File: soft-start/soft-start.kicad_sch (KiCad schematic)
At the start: 29 parts, among them M1 Motor_DC, Q1 IRFB3004PbF, SW1 L1's relay switch, U1 4011, U2 CD4060BE

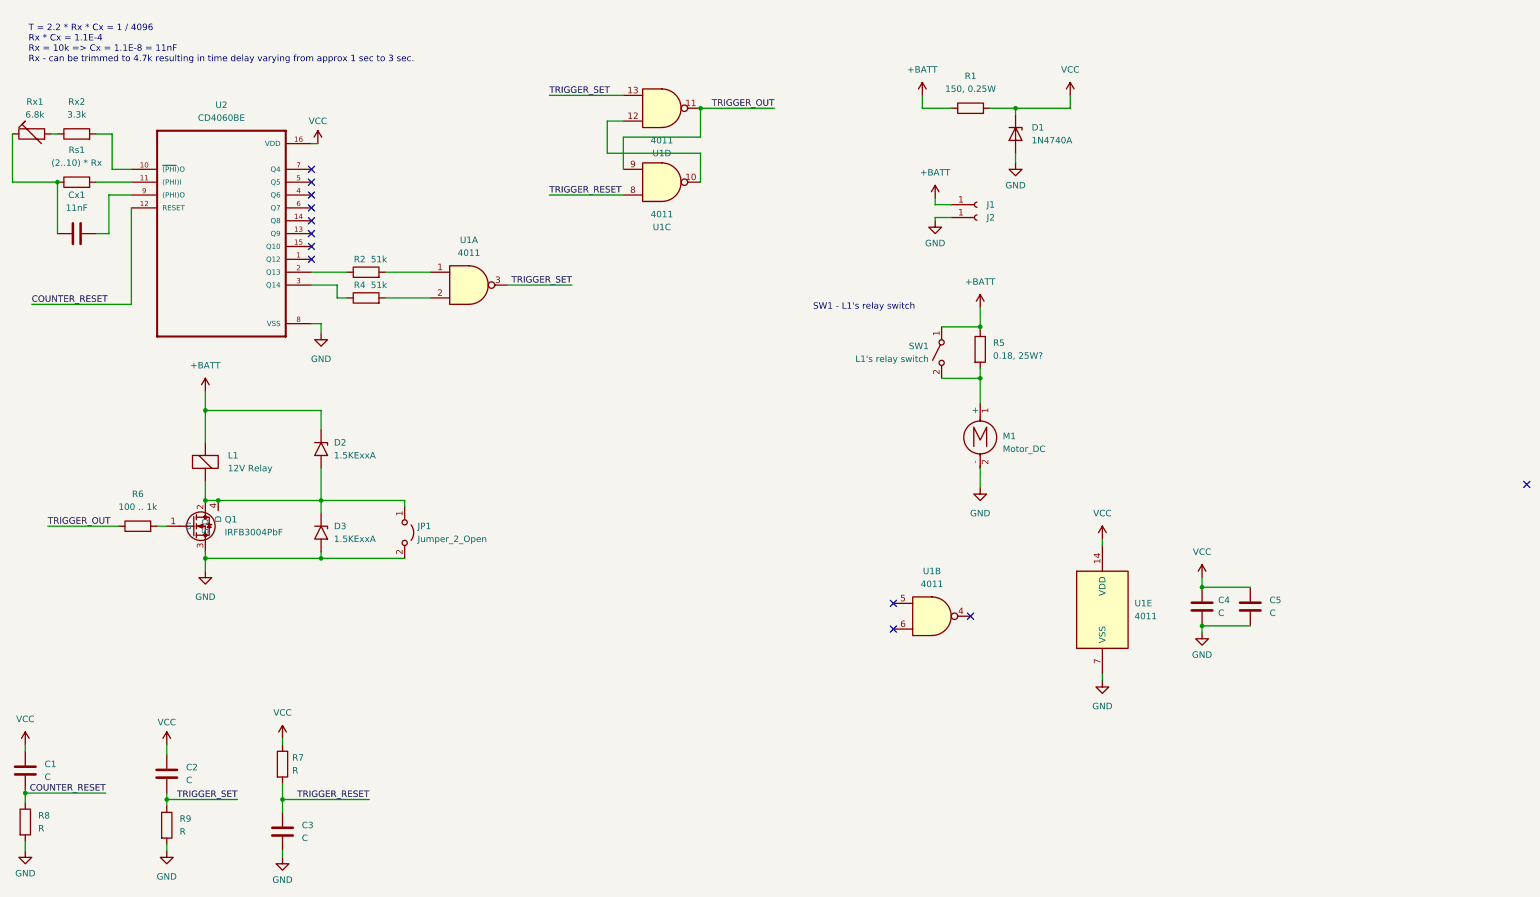
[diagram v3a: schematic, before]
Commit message: [soft-start] Update schematic and add PCB
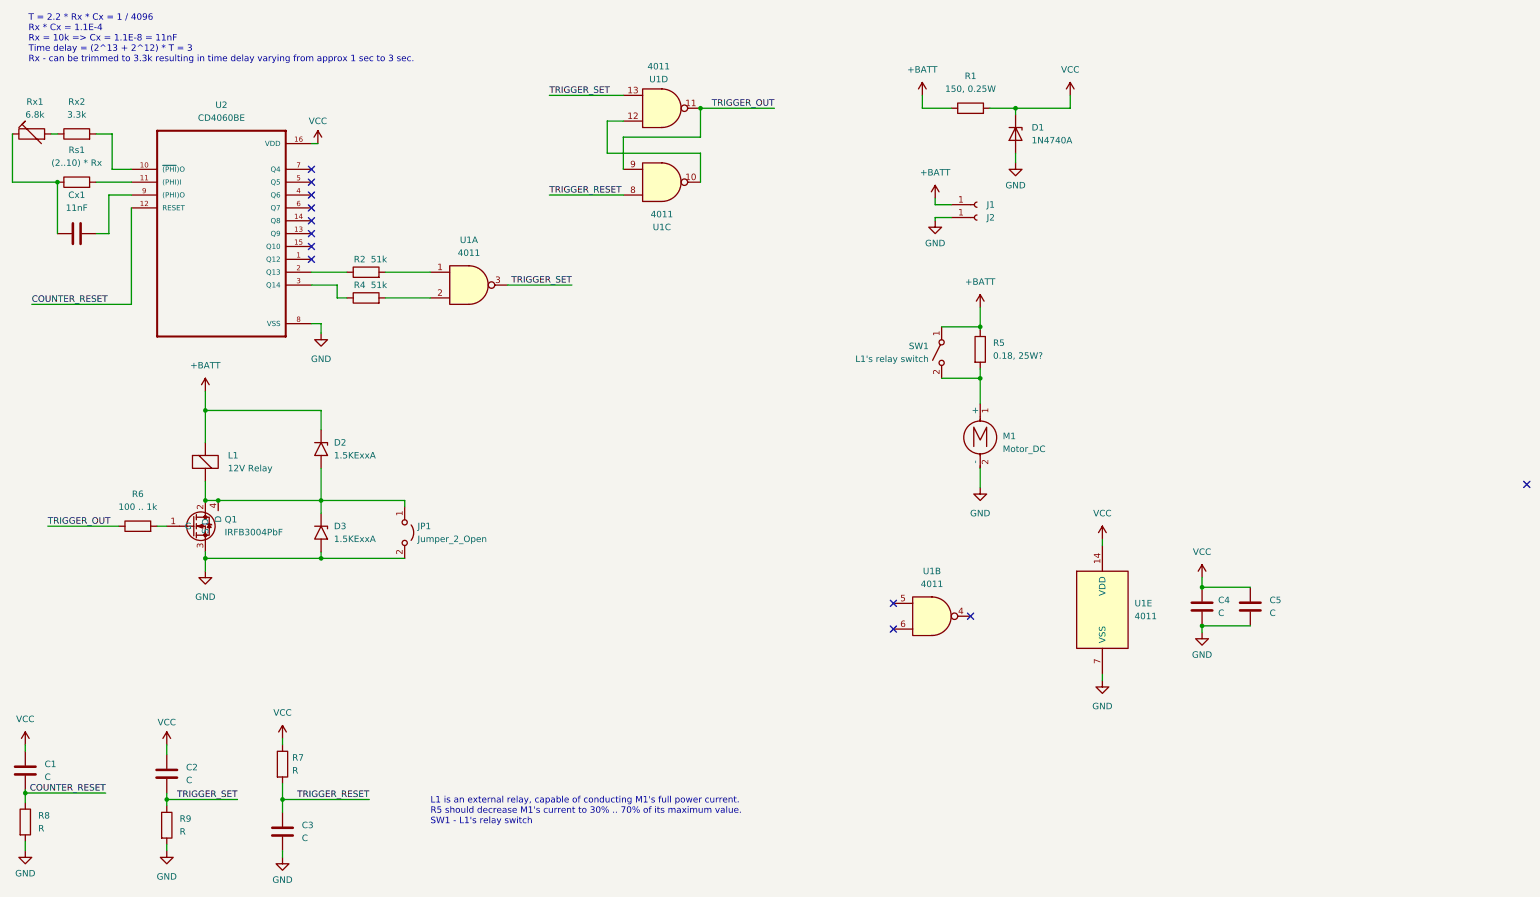
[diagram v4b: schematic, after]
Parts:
- L1: footprint (none) -> Connector_Wire:SolderWire-1.5sqmm_1x02_P6mm_D1.7mm_OD3mm
- R7: footprint Resistor_THT:R_Axial_DIN0207_L6.3mm_D2.5mm_P2.54mm_Vertical -> Resistor_THT:R_Axial_DIN0207_L6.3mm_D2.5mm_P7.62mm_Horizontal
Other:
- note added: "L1 is an external relay, capable of conducting M1's full power current. R5 should decrease M1's current to 30% .. 70% of its maximum value. SW1 - L1's relay switch"
- note added: "T = 2.2 * Rx * Cx = 1 / 4096 Rx * Cx = 1.1E-4 Rx = 10k => Cx = 1.1E-8 = 11nF Time delay = (2^13 + 2^12) * T = 3 Rx - can be trimmed to 3.3k resulting in time delay varying from approx 1 sec to 3 sec."
- note removed: "SW1 - L1's relay switch"
- note removed: "T = 2.2 * Rx * Cx = 1 / 4096 Rx * Cx = 1.1E-4 Rx = 10k => Cx = 1.1E-8 = 11nF Rx - can be trimmed to 4.7k resulting in time delay varying from approx 1 sec to 3 sec."
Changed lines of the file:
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@@
     (stroke (width 0) (type default))
   )
-  (text "T = 2.2 * Rx * Cx = 1 / 4096\nRx * Cx = 1.1E-4\nRx = 10k => Cx = 1.1E-8 = 11nF\nRx - can be trimmed to 4.7k resulting in time delay varying from approx 1 sec to 3 sec."
+  (text "T = 2.2 * Rx * Cx = 1 / 4096\nRx * Cx = 1.1E-4\nRx = 10k => Cx = 1.1E-8 = 11nF\nTime delay = (2^13 + 2^12) * T = 3\nRx - can be trimmed to 3.3k resulting in time delay varying from approx 1 sec to 3 sec.\n"
     (at 25.4 24.13 0)
     (effects (font (size 1.27 1.27)) (justify left bottom))
   )
-  (text "SW1 - L1's relay switch" (at 180.34 73.025 0)
+  (text "L1 is an external relay, capable of conducting M1's full power current.\nR5 should decrease M1's current to 30% .. 70% of its maximum value.\nSW1 - L1's relay switch"
+    (at 104.775 174.625 0)
     (effects (font (size 1.27 1.27)) (justify left bottom))
   )
@@
   (symbol (lib_id "4xxx:4011") (at 150.495 33.02 0) (mirror x) (unit 4)
     (in_bom yes) (on_board yes) (dnp no)
-    (property "Reference" "U1" (at 150.4867 41.91 0)
-      (effects (font (size 1.27 1.27)))
-    )
-    (property "Value" "4011" (at 150.4867 39.37 0)
+    (property "Reference" "U1" (at 149.86 27.305 0)
+      (effects (font (size 1.27 1.27)))
+    )
+    (property "Value" "4011" (at 149.86 24.765 0)
       (effects (font (size 1.27 1.27)))
     )
@@
       (effects (font (size 1.27 1.27)) (justify left))
     )
-    (property "Footprint" "Resistor_THT:R_Axial_DIN0207_L6.3mm_D2.5mm_P2.54mm_Vertical" (at 73.787 162.56 90)
+    (property "Footprint" "Resistor_THT:R_Axial_DIN0207_L6.3mm_D2.5mm_P7.62mm_Horizontal" (at 73.787 162.56 90)
       (effects (font (size 1.27 1.27)) hide)
     )
@@
   )
   (symbol (lib_id "Device:ElectromagneticActor") (at 60.325 104.14 0) (unit 1)
-    (in_bom no) (on_board no) (dnp no) (fields_autoplaced)
+    (in_bom no) (on_board yes) (dnp no) (fields_autoplaced)
     (property "Reference" "L1" (at 64.77 101.6 0)
       (effects (font (size 1.27 1.27)) (justify left))
@@
       (effects (font (size 1.27 1.27)) (justify left))
     )
-    (property "Footprint" "" (at 59.69 101.6 90)
-      (effects (font (size 1.27 1.27)) hide)
-    )
+    (property "Footprint" "Connector_Wire:SolderWire-1.5sqmm_1x02_P6mm_D1.7mm_OD3mm" (at 59.69 101.6 90)
+      (effects (font (size 1.27 1.27)) hide)
+    )

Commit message: [soft-start] Update PCB - decrease dimensions, remove hard tracks.
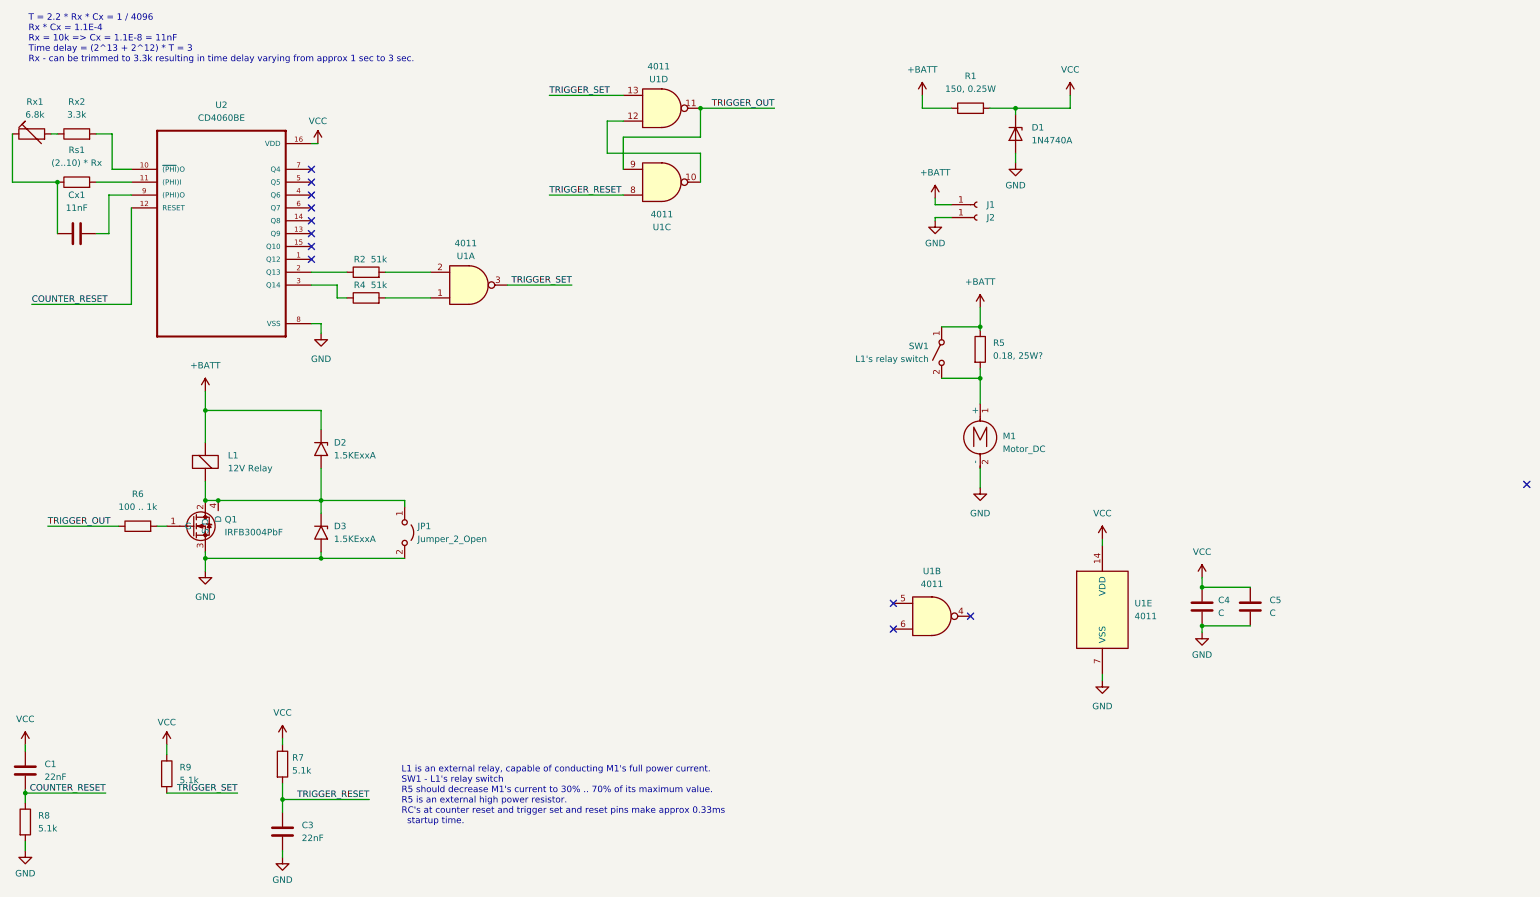
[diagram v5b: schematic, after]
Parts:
- removed C2: C, Capacitor_THT:C_Disc_D6.0mm_W4.4mm_P5.00mm, symbol Device:C
- C1, C3: value C -> 22nF
- R1, R2, R4: footprint Resistor_THT:R_Axial_DIN0207_L6.3mm_D2.5mm_P2.54mm_Vertical -> Resistor_THT:R_Axial_DIN0207_L6.3mm_D2.5mm_P7.62mm_Horizontal
- R7, R8, R9: value R -> 5.1k
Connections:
- net GND: no longer R9.2
- net TRIGGER_SET: now also R9.2; no longer R9.1
- net VCC: now also R9.1
- net at R4.2: now also U1.1; no longer U1.2
- net at R2.2: now also U1.2; no longer U1.1
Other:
- note added: "L1 is an external relay, capable of conducting M1's full power current. SW1 - L1's relay switch R5 should decrease M1's current to 30% .. 70% of its maximum value. R5 is an external high power resistor. RC's at counter reset and trigger set and reset pins make approx 0.33ms startup time."
- note removed: "L1 is an external relay, capable of conducting M1's full power current. R5 should decrease M1's current to 30% .. 70% of its maximum value. SW1 - L1's relay switch"
- moved on the sheet: R9
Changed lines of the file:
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@@
   (junction (at 83.185 110.49) (diameter 0) (color 0 0 0 0)
-  )
-  (junction (at 52.705 169.545) (diameter 0) (color 0 0 0 0)
   )
   (junction (at 83.185 121.92) (diameter 0) (color 0 0 0 0)
@@
     (stroke (width 0) (type default))
   )
-  (wire (pts (xy 52.705 169.545) (xy 52.705 170.815))
-    (stroke (width 0) (type default))
-  )
   (wire (pts (xy 139.7 41.91) (xy 139.7 35.56))
     (stroke (width 0) (type default))
@@
     (stroke (width 0) (type default))
   )
-  (wire (pts (xy 52.705 178.435) (xy 52.705 179.705))
-    (stroke (width 0) (type default))
-  )
   (wire (pts (xy 86.36 67.945) (xy 86.36 70.485))
     (stroke (width 0) (type default))
@@
     (stroke (width 0) (type default))
   )
-  (wire (pts (xy 52.705 169.545) (xy 66.675 169.545))
+  (wire (pts (xy 52.705 168.275) (xy 66.675 168.275))
     (stroke (width 0) (type default))
   )
@@
   )
   (wire (pts (xy 24.765 158.75) (xy 24.765 160.02))
-    (stroke (width 0) (type default))
-  )
-  (wire (pts (xy 52.705 168.275) (xy 52.705 169.545))
     (stroke (width 0) (type default))
   )
@@
     (effects (font (size 1.27 1.27)) (justify left bottom))
   )
-  (text "L1 is an external relay, capable of conducting M1's full power current.\nR5 should decrease M1's current to 30% .. 70% of its maximum value.\nSW1 - L1's relay switch"
-    (at 104.775 174.625 0)
+  (text "L1 is an external relay, capable of conducting M1's full power current.\nSW1 - L1's relay switch\nR5 should decrease M1's current to 30% .. 70% of its maximum value.\nR5 is an external high power resistor.\nRC's at counter reset and trigger set and reset pins make approx 0.33ms\n  startup time."
+    (at 99.06 174.625 0)
     (effects (font (size 1.27 1.27)) (justify left bottom))
   )
@@
     (effects (font (size 1.27 1.27)) (justify left bottom))
   )
-  (label "TRIGGER_SET" (at 66.675 169.545 180) (fields_autoplaced)
+  (label "TRIGGER_SET" (at 66.675 168.275 180) (fields_autoplaced)
     (effects (font (size 1.27 1.27)) (justify right bottom))
   )
@@
       (effects (font (size 1.27 1.27)) (justify left))
     )
-    (property "Value" "R" (at 27.305 175.26 0)
+    (property "Value" "5.1k" (at 27.305 175.26 0)
       (effects (font (size 1.27 1.27)) (justify left))
     )
@@
       (effects (font (size 1.27 1.27)) (justify left))
     )
-    (property "Value" "C" (at 79.375 177.165 0)
+    (property "Value" "22nF" (at 79.375 177.165 0)
       (effects (font (size 1.27 1.27)) (justify left))
     )
@@
     )
   )
-  (symbol (lib_id "Device:R") (at 52.705 174.625 0) (unit 1)
-    (in_bom yes) (on_board yes) (dnp no) (fields_autoplaced)
-    (property "Reference" "R9" (at 55.245 173.355 0)
-      (effects (font (size 1.27 1.27)) (justify left))
-    )
-    (property "Value" "R" (at 55.245 175.895 0)
-      (effects (font (size 1.27 1.27)) (justify left))
-    )
-    (property "Footprint" "Resistor_THT:R_Axial_DIN0207_L6.3mm_D2.5mm_P2.54mm_Vertical" (at 50.927 174.625 90)
-      (effects (font (size 1.27 1.27)) hide)
-    )
-    (property "Datasheet" "~" (at 52.705 174.625 0)
+  (symbol (lib_id "Device:R") (at 52.705 164.465 0) (unit 1)
+    (in_bom yes) (on_board yes) (dnp no) (fields_autoplaced)
+    (property "Reference" "R9" (at 55.245 163.195 0)
+      (effects (font (size 1.27 1.27)) (justify left))
+    )
+    (property "Value" "5.1k" (at 55.245 165.735 0)
+      (effects (font (size 1.27 1.27)) (justify left))
+    )
+    (property "Footprint" "Resistor_THT:R_Axial_DIN0207_L6.3mm_D2.5mm_P2.54mm_Vertical" (at 50.927 164.465 90)
+      (effects (font (size 1.27 1.27)) hide)
+    )
+    (property "Datasheet" "~" (at 52.705 164.465 0)
       (effects (font (size 1.27 1.27)) hide)
     )
@@
   )
   (symbol (lib_id "Device:R") (at 213.36 80.645 0) (unit 1)
-    (in_bom yes) (on_board yes) (dnp no) (fields_autoplaced)
+    (in_bom yes) (on_board no) (dnp no) (fields_autoplaced)
     (property "Reference" "R5" (at 215.9 79.375 0)
       (effects (font (size 1.27 1.27)) (justify left))
@@
       (effects (font (size 1.27 1.27)))
     )
-    (property "Footprint" "Resistor_THT:R_Axial_DIN0207_L6.3mm_D2.5mm_P2.54mm_Vertical" (at 92.075 72.263 90)
+    (property "Footprint" "Resistor_THT:R_Axial_DIN0207_L6.3mm_D2.5mm_P7.62mm_Horizontal" (at 92.075 72.263 90)
       (effects (font (size 1.27 1.27)) hide)
     )
@@
     )
   )
-  (symbol (lib_id "Device:C") (at 52.705 164.465 0) (unit 1)
-    (in_bom yes) (on_board yes) (dnp no) (fields_autoplaced)
-    (property "Reference" "C2" (at 56.515 163.195 0)
-      (effects (font (size 1.27 1.27)) (justify left))
-    )
-    (property "Value" "C" (at 56.515 165.735 0)
-      (effects (font (size 1.27 1.27)) (justify left))
-    )
-    (property "Footprint" "Capacitor_THT:C_Disc_D6.0mm_W4.4mm_P5.00mm" (at 53.6702 168.275 0)
-      (effects (font (size 1.27 1.27)) hide)
-    )
-    (property "Datasheet" "~" (at 52.705 164.465 0)
-      (effects (font (size 1.27 1.27)) hide)
-    )
-    (pin "1")
-    (pin "2")
-    (instances
-      (project "soft-start"
-        (path "/dd3da890-32ef-4a5a-aea4-e5d2141f1ff1"
-          (reference "C2") (unit 1)
-        )
-      )
-    )
-  )
   (symbol (lib_id "Switch:SW_SPST") (at 205.74 81.28 90) (mirror x) (unit 1)
     (in_bom no) (on_board no) (dnp no)
@@
     )
   )
-  (symbol (lib_name "GND_3") (lib_id "power:GND") (at 52.705 179.705 0) (unit 1)
-    (in_bom yes) (on_board yes) (dnp no) (fields_autoplaced)
-    (property "Reference" "#PWR012" (at 52.705 186.055 0)
-      (effects (font (size 1.27 1.27)) hide)
-    )
-    (property "Value" "GND" (at 52.705 184.785 0)
-      (effects (font (size 1.27 1.27)))
-    )
-    (property "Footprint" "" (at 52.705 179.705 0)
-      (effects (font (size 1.27 1.27)) hide)
-    )
-    (property "Datasheet" "" (at 52.705 179.705 0)
-      (effects (font (size 1.27 1.27)) hide)
-    )
-    (pin "1")
-    (instances
-      (project "soft-start"
-        (path "/dd3da890-32ef-4a5a-aea4-e5d2141f1ff1"
-          (reference "#PWR012") (unit 1)
-        )
-      )
-    )
-  )
   (symbol (lib_id "power:GND") (at 60.325 124.46 0) (unit 1)
     (in_bom yes) (on_board yes) (dnp no) (fields_autoplaced)
@@
       (effects (font (size 1.27 1.27)) (justify left))
     )
-    (property "Value" "R" (at 77.47 163.83 0)
+    (property "Value" "5.1k" (at 77.47 163.83 0)
       (effects (font (size 1.27 1.27)) (justify left))
     )
@@
       (effects (font (size 1.27 1.27)) (justify left))
     )
-    (property "Value" "C" (at 28.575 165.1 0)
+    (property "Value" "22nF" (at 28.575 165.1 0)
       (effects (font (size 1.27 1.27)) (justify left))
     )
@@
     )
   )
-  (symbol (lib_id "4xxx:4011") (at 112.395 67.945 0) (unit 1)
-    (in_bom yes) (on_board yes) (dnp no) (fields_autoplaced)
-    (property "Reference" "U1" (at 112.3867 59.055 0)
-      (effects (font (size 1.27 1.27)))
-    )
-    (property "Value" "4011" (at 112.3867 61.595 0)
+  (symbol (lib_id "4xxx:4011") (at 112.395 67.945 0) (mirror x) (unit 1)
+    (in_bom yes) (on_board yes) (dnp no)
+    (property "Reference" "U1" (at 111.76 62.23 0)
+      (effects (font (size 1.27 1.27)))
+    )
+    (property "Value" "4011" (at 111.76 59.69 0)
       (effects (font (size 1.27 1.27)))
     )
@@
       (effects (font (size 1.27 1.27)))
     )
-    (property "Footprint" "Resistor_THT:R_Axial_DIN0207_L6.3mm_D2.5mm_P2.54mm_Vertical" (at 211.455 34.798 90)
+    (property "Footprint" "Resistor_THT:R_Axial_DIN0207_L6.3mm_D2.5mm_P7.62mm_Horizontal" (at 211.455 34.798 90)
       (effects (font (size 1.27 1.27)) hide)
     )
@@
       (effects (font (size 1.27 1.27)))
     )
-    (property "Footprint" "Resistor_THT:R_Axial_DIN0207_L6.3mm_D2.5mm_P2.54mm_Vertical" (at 92.075 67.183 90)
-      (effects (font (size 1.27 1.27)) hide)
-    )
+    (property "Footprint" "Resistor_THT:R_Axial_DIN0207_L6.3mm_D2.5mm_P7.62mm_Horizontal" (at 92.075 67.183 90)
+      (effects (font (size 1.27 1.27)) hide)
+    )
